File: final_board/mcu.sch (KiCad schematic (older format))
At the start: 9 parts, among them U402 MCP2551-I/SN, U403 LPC11C14

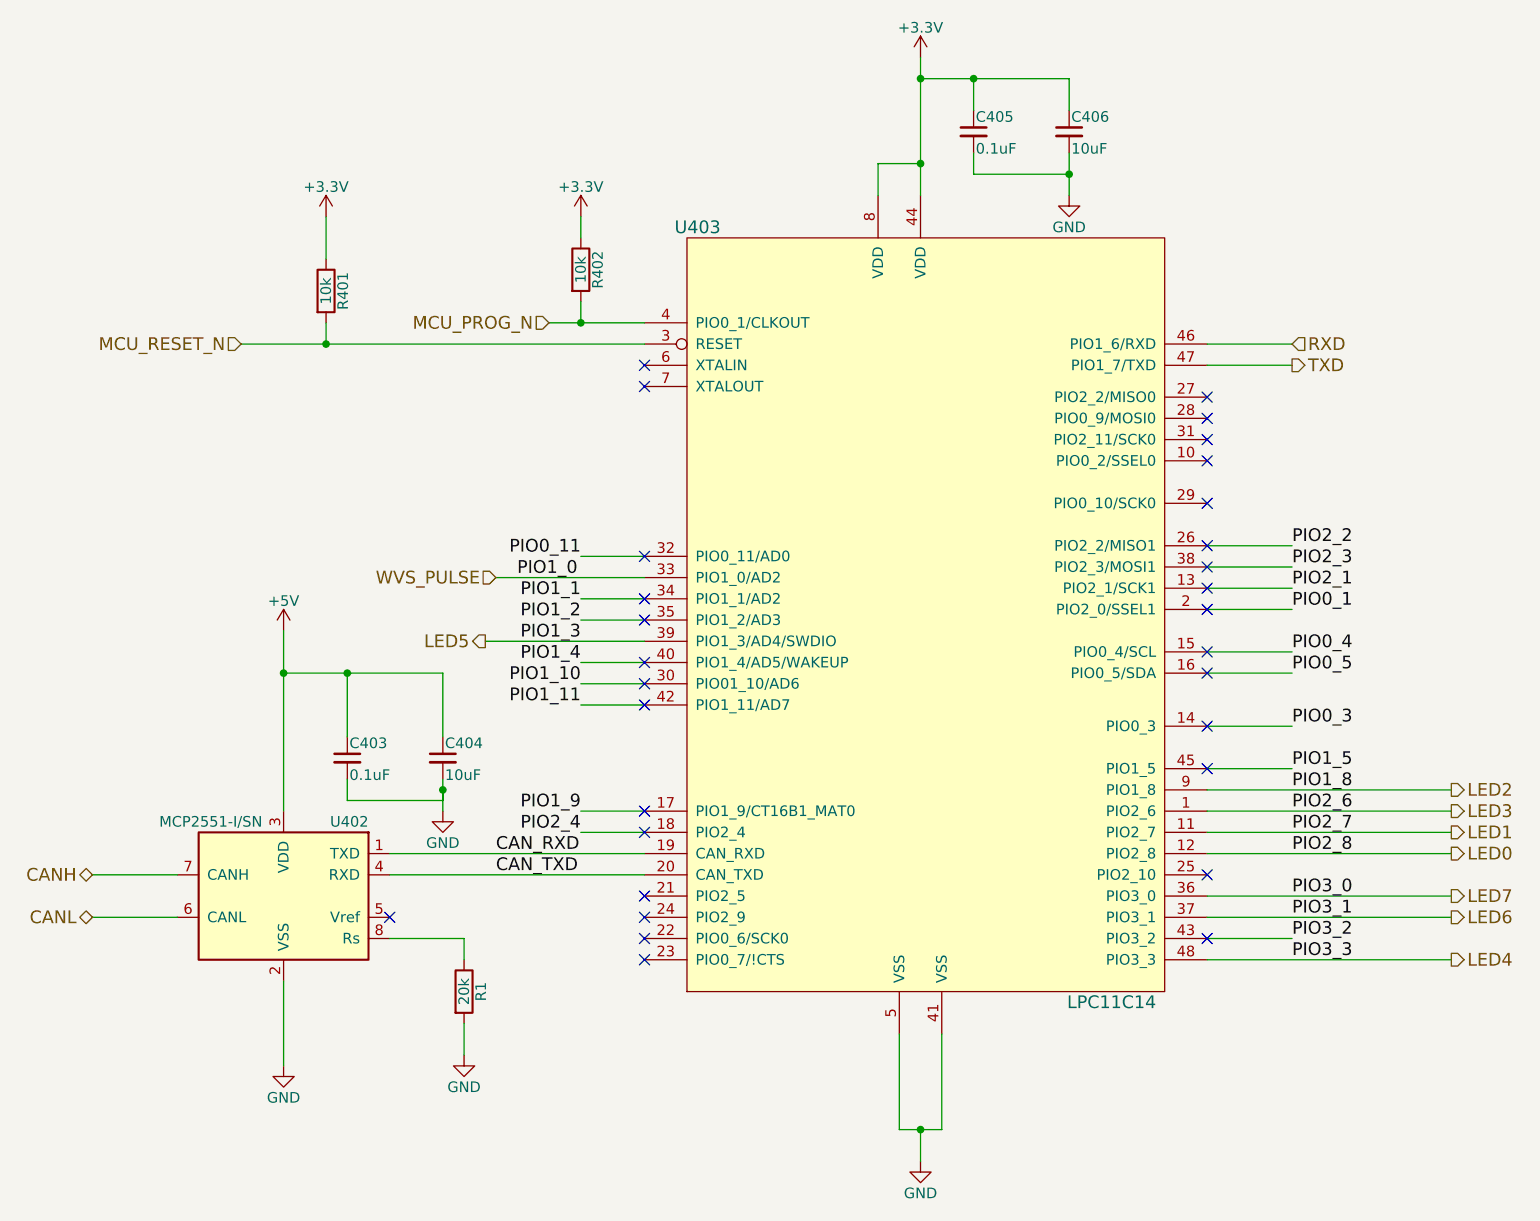
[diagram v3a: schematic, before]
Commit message: Updated PCB by replacing old parts, fixing voltage regulator, adding test points, and general improvements
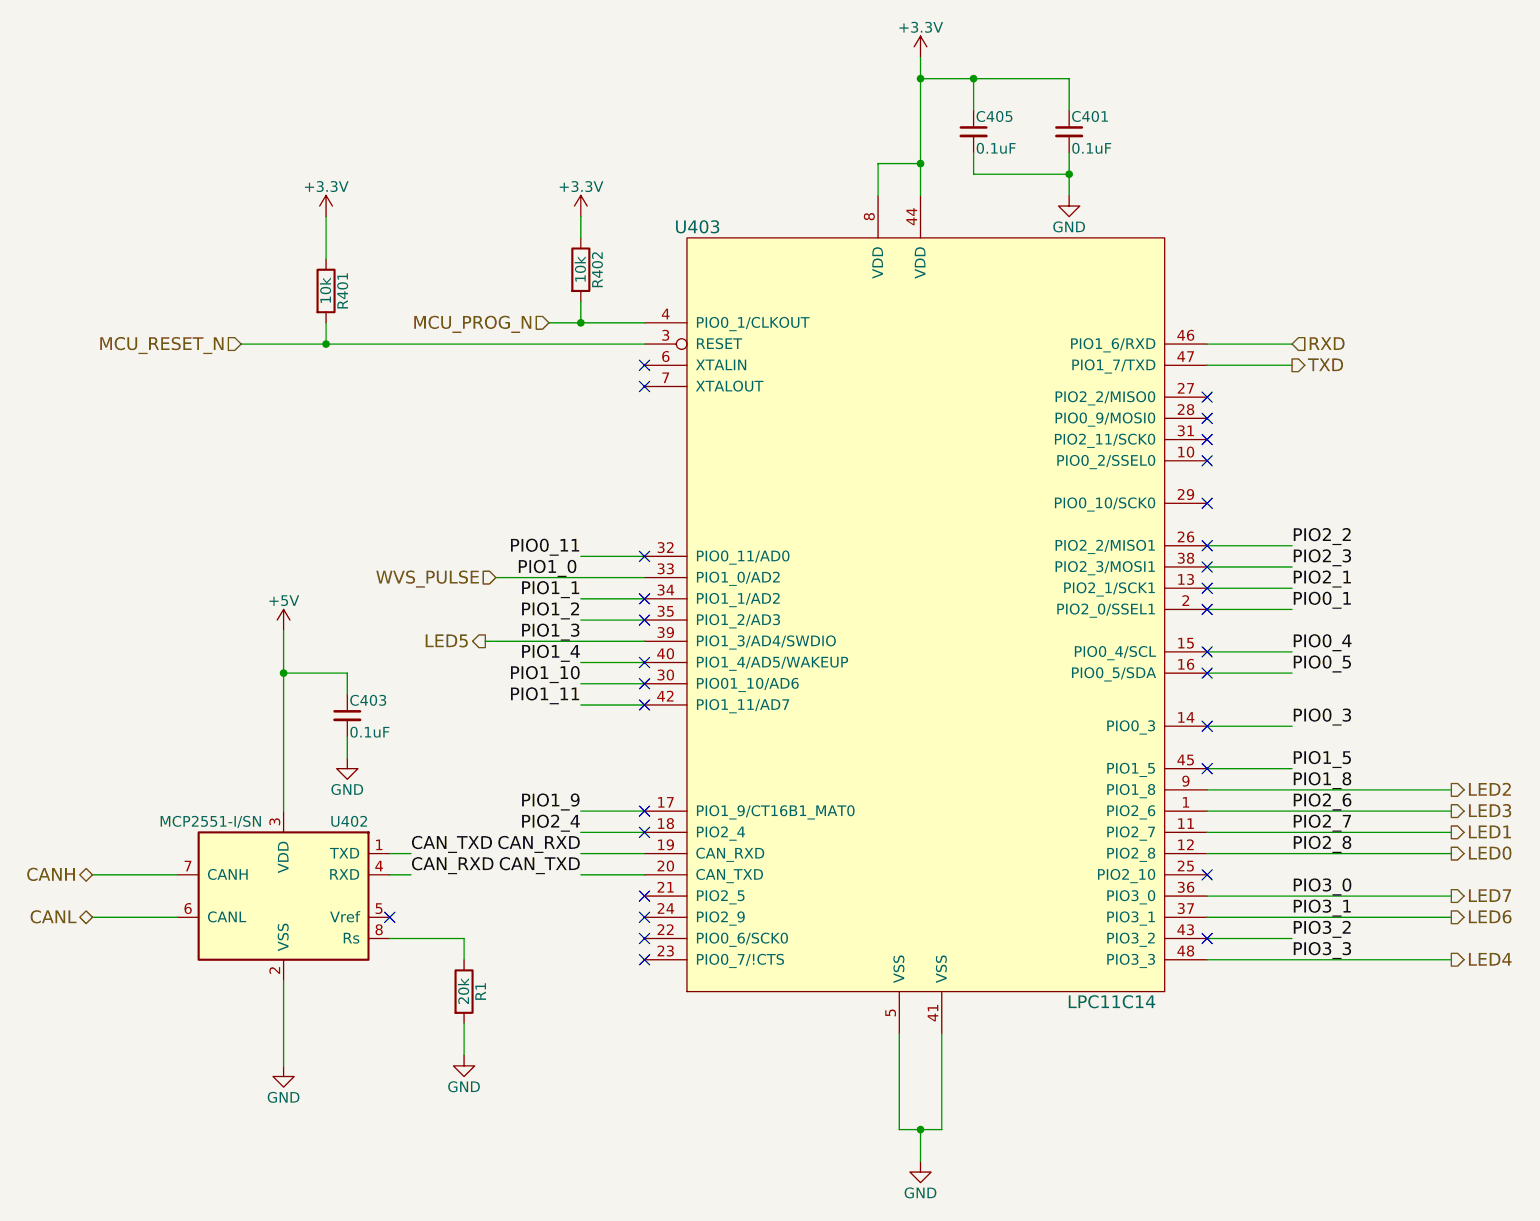
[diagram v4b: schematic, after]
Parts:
- removed C404, C406: 10uF, Capacitors_SMD:C_0805_HandSoldering, symbol C_Small
- added C401: 0.1uF, Capacitors_SMD:C_0603_HandSoldering, symbol C_Small
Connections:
- net +3V3: now also C401.1
- net CAN_RXD: now also U402.4 (RXD); no longer U402.1 (TXD)
- net CAN_TXD: now also U402.1 (TXD); no longer U402.4 (RXD)
- net GND: now also C401.2
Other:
- moved on the sheet: C403
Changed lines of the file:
@@
 CANH
 $Comp
-L GND #PWR09
+L GND #PWR017
 U 1 1 563E2693
 P 4100 5700
-F 0 "#PWR09" H 4100 5450 50  0001 C CNN
+F 0 "#PWR017" H 4100 5450 50  0001 C CNN
 F 1 "GND" H 4100 5550 50  0000 C CNN
 F 2 "" H 4100 5700 60  0000 C CNN
@@
 $EndComp
 $Comp
-L GND #PWR010
+L GND #PWR018
 U 1 1 563E26E3
 P 3250 5750
-F 0 "#PWR010" H 3250 5500 50  0001 C CNN
+F 0 "#PWR018" H 3250 5500 50  0001 C CNN
 F 1 "GND" H 3250 5600 50  0000 C CNN
 F 2 "" H 3250 5750 60  0000 C CNN
@@
 L C_Small C403
 U 1 1 563E286E
+P 3550 4100
+F 0 "C403" H 3560 4170 50  0000 L CNN
+F 1 "0.1uF" H 3560 4020 50  0000 L CNN
+F 2 "Capacitors_SMD:C_0603_HandSoldering" H 3550 4100 60  0001 C CNN
+F 3 "" H 3550 4100 60  0000 C CNN
+	1    3550 4100
+	1    0    0    -1
+$EndComp
+$Comp
+L GND #PWR019
+U 1 1 563E2AAC
 P 3550 4300
-F 0 "C403" H 3560 4370 50  0000 L CNN
-F 1 "0.1uF" H 3560 4220 50  0000 L CNN
-F 2 "Capacitors_SMD:C_0603_HandSoldering" H 3550 4300 60  0001 C CNN
+F 0 "#PWR019" H 3550 4050 50  0001 C CNN
+F 1 "GND" H 3550 4150 50  0000 C CNN
+F 2 "" H 3550 4300 60  0000 C CNN
 F 3 "" H 3550 4300 60  0000 C CNN
 	1    3550 4300
-	1    0    0    -1
-$EndComp
-$Comp
-L C_Small C404
-U 1 1 563E28A1
-P 4000 4300
-F 0 "C404" H 4010 4370 50  0000 L CNN
-F 1 "10uF" H 4010 4220 50  0000 L CNN
-F 2 "Capacitors_SMD:C_0805_HandSoldering" H 4000 4300 60  0001 C CNN
-F 3 "" H 4000 4300 60  0000 C CNN
-	1    4000 4300
-	1    0    0    -1
-$EndComp
-$Comp
-L GND #PWR011
-U 1 1 563E2AAC
-P 4000 4550
-F 0 "#PWR011" H 4000 4300 50  0001 C CNN
-F 1 "GND" H 4000 4400 50  0000 C CNN
-F 2 "" H 4000 4550 60  0000 C CNN
-F 3 "" H 4000 4550 60  0000 C CNN
-	1    4000 4550
 	1    0    0    -1
 $EndComp
@@
 PIO2_4
 $Comp
-L GND #PWR012
+L GND #PWR020
 U 1 1 563E497F
 P 6250 6200
-F 0 "#PWR012" H 6250 5950 50  0001 C CNN
+F 0 "#PWR020" H 6250 5950 50  0001 C CNN
 F 1 "GND" H 6250 6050 50  0000 C CNN
 F 2 "" H 6250 6200 60  0000 C CNN
@@
 $EndComp
 $Comp
-L C_Small C406
-U 1 1 563E4C7A
-P 6950 1350
-F 0 "C406" H 6960 1420 50  0000 L CNN
-F 1 "10uF" H 6960 1270 50  0000 L CNN
-F 2 "Capacitors_SMD:C_0805_HandSoldering" H 6950 1350 60  0001 C CNN
-F 3 "" H 6950 1350 60  0000 C CNN
-	1    6950 1350
-	1    0    0    -1
-$EndComp
-$Comp
-L GND #PWR013
+L GND #PWR021
 U 1 1 563E4F46
 P 6950 1650
-F 0 "#PWR013" H 6950 1400 50  0001 C CNN
+F 0 "#PWR021" H 6950 1400 50  0001 C CNN
 F 1 "GND" H 6950 1500 50  0000 C CNN
 F 2 "" H 6950 1650 60  0000 C CNN
@@
 LED0
 $Comp
-L +3.3V #PWR014
+L +3.3V #PWR022
 U 1 1 5647852E
 P 3450 1750
-F 0 "#PWR014" H 3450 1600 50  0001 C CNN
+F 0 "#PWR022" H 3450 1600 50  0001 C CNN
 F 1 "+3.3V" H 3450 1890 50  0000 C CNN
 F 2 "" H 3450 1750 60  0000 C CNN
@@
 $EndComp
 $Comp
-L +3.3V #PWR015
+L +3.3V #PWR023
 U 1 1 56478628
 P 4650 1750
-F 0 "#PWR015" H 4650 1600 50  0001 C CNN
+F 0 "#PWR023" H 4650 1600 50  0001 C CNN
 F 1 "+3.3V" H 4650 1890 50  0000 C CNN
 F 2 "" H 4650 1750 60  0000 C CNN
@@
 $EndComp
 $Comp
-L +3.3V #PWR016
+L +3.3V #PWR024
 U 1 1 56478697
 P 6250 1000
-F 0 "#PWR016" H 6250 850 50  0001 C CNN
+F 0 "#PWR024" H 6250 850 50  0001 C CNN
 F 1 "+3.3V" H 6250 1140 50  0000 C CNN
 F 2 "" H 6250 1000 60  0000 C CNN
@@
 	1    0    0    -1
 $EndComp
-Text Label 4250 4750 0    60   ~ 0
+Text Label 4650 4750 2    60   ~ 0
 CAN_RXD
-Text Label 4250 4850 0    60   ~ 0
+Text Label 4650 4850 2    60   ~ 0
 CAN_TXD
 Text Label 4650 3750 2    60   ~ 0
 PIO1_3
-Wire Wire Line
-	3750 4750 4950 4750
-Wire Wire Line
-	3750 4850 4950 4850
-Wire Wire Line
-	2350 4850 2750 4850
-Wire Wire Line
-	2350 5050 2750 5050
-Wire Wire Line
-	3250 3700 3250 4550
-Wire Wire Line
-	3550 3900 3550 4200
-Wire Wire Line
-	4000 3900 4000 4200
-Connection ~ 3550 3900
-Wire Wire Line
-	3550 4400 3550 4500
-Wire Wire Line
-	3550 4500 4000 4500
-Wire Wire Line
-	4000 4500 4000 4400
-Wire Wire Line
-	4000 4450 4000 4550
-Connection ~ 4000 4450
-Connection ~ 3250 3900
-Wire Wire Line
-	4950 4050 4650 4050
-Wire Wire Line
-	4650 3950 4950 3950
-Wire Wire Line
-	4650 3350 4950 3350
-Wire Wire Line
-	4250 3450 4950 3450
-Wire Wire Line
-	4650 3550 4950 3550
-Wire Wire Line
-	4650 3650 4950 3650
-Wire Wire Line
-	4200 3750 4950 3750
-Wire Wire Line
-	4650 3850 4950 3850
-Wire Wire Line
-	4500 2250 4950 2250
-Wire Wire Line
-	4650 2150 4650 2250
-Connection ~ 4650 2250
-Wire Wire Line
-	4650 1850 4650 1750
-Wire Wire Line
-	3050 2350 4950 2350
-Wire Wire Line
-	3450 2250 3450 2350
-Connection ~ 3450 2350
-Wire Wire Line
-	3450 1750 3450 1950
-Wire Wire Line
-	4650 4550 4950 4550
-Wire Wire Line
-	4650 4650 4950 4650
-Wire Wire Line
-	6150 5600 6150 6050
-Wire Wire Line
-	6150 6050 6350 6050
-Wire Wire Line
-	6350 6050 6350 5600
-Wire Wire Line
-	6250 6050 6250 6200
-Connection ~ 6250 6050
-Wire Wire Line
-	6250 1000 6250 1650
-Wire Wire Line
-	6050 1650 6050 1500
-Wire Wire Line
-	6050 1500 6250 1500
-Connection ~ 6250 1500
-Wire Wire Line
-	6250 1100 6950 1100
-Wire Wire Line
-	6950 1100 6950 1250
-Connection ~ 6250 1100
-Wire Wire Line
-	6500 1250 6500 1100
-Connection ~ 6500 1100
-Wire Wire Line
-	6950 1450 6950 1650
-Wire Wire Line
-	6950 1550 6500 1550
-Wire Wire Line
-	6500 1550 6500 1450
-Connection ~ 6950 1550
-Wire Wire Line
-	8000 2350 7600 2350
-Wire Wire Line
-	8000 2450 7600 2450
-Wire Wire Line
-	8000 3300 7600 3300
-Wire Wire Line
-	7600 3400 8000 3400
-Wire Wire Line
-	7600 3500 8000 3500
-Wire Wire Line
-	7600 3600 8000 3600
-Wire Wire Line
-	8000 3800 7600 3800
-Wire Wire Line
-	8000 3900 7600 3900
-Wire Wire Line
-	8000 4150 7600 4150
-Wire Wire Line
-	8000 4350 7600 4350
-Wire Wire Line
-	7600 4450 8750 4450
-Wire Wire Line
-	7600 4550 8750 4550
-Wire Wire Line
-	7600 4650 8750 4650
-Wire Wire Line
-	7600 4750 8750 4750
-Wire Wire Line
-	7600 4950 8750 4950
-Wire Wire Line
-	7600 5050 8750 5050
-Wire Wire Line
-	7600 5150 8000 5150
-Wire Wire Line
-	7600 5250 8750 5250
 Text HLabel 4250 3450 0    60   Input ~ 0
 WVS_PULSE
@@
 	-1   0    0    -1
 $EndComp
-Wire Wire Line
-	3250 5350 3250 5750
-Wire Wire Line
-	3250 3900 4000 3900
 $Comp
 L R R1
@@
 	1    0    0    -1
 $EndComp
-Wire Wire Line
-	4100 5550 4100 5700
 NoConn ~ 3750 5050
-Wire Wire Line
-	3750 5150 4100 5150
-Wire Wire Line
-	4100 5150 4100 5250
-$Comp
-L +5V #PWR017
+$Comp
+L +5V #PWR025
 U 1 1 56917D77
 P 3250 3700
-F 0 "#PWR017" H 3250 3550 50  0001 C CNN
+F 0 "#PWR025" H 3250 3550 50  0001 C CNN
 F 1 "+5V" H 3250 3840 50  0000 C CNN
 F 2 "" H 3250 3700 50  0000 C CNN
@@
 NoConn ~ 4950 3550
 NoConn ~ 4950 3350
+$Comp
+L C_Small C401
+U 1 1 5825915E
+P 6950 1350
+F 0 "C401" H 6960 1420 50  0000 L CNN
+F 1 "0.1uF" H 6960 1270 50  0000 L CNN
+F 2 "Capacitors_SMD:C_0603_HandSoldering" H 6950 1350 50  0001 C CNN
+F 3 "" H 6950 1350 50  0000 C CNN
+	1    6950 1350
+	1    0    0    -1
+$EndComp
+Wire Wire Line
+	2350 4850 2750 4850
+Wire Wire Line
+	2350 5050 2750 5050
+Wire Wire Line
+	3250 3700 3250 4550
+Connection ~ 3250 3900
+Wire Wire Line
+	4950 4050 4650 4050
+Wire Wire Line
+	4650 3950 4950 3950
+Wire Wire Line
+	4650 3350 4950 3350
+Wire Wire Line
+	4250 3450 4950 3450
+Wire Wire Line
+	4650 3550 4950 3550
+Wire Wire Line
+	4650 3650 4950 3650
+Wire Wire Line
+	4200 3750 4950 3750
+Wire Wire Line
+	4650 3850 4950 3850
+Wire Wire Line
+	4500 2250 4950 2250
+Wire Wire Line
+	4650 2150 4650 2250
+Connection ~ 4650 2250
+Wire Wire Line
+	4650 1850 4650 1750
+Wire Wire Line
+	3050 2350 4950 2350
+Wire Wire Line
+	3450 2250 3450 2350
+Connection ~ 3450 2350
+Wire Wire Line
+	3450 1750 3450 1950
+Wire Wire Line
+	4650 4550 4950 4550
+Wire Wire Line
+	4650 4650 4950 4650
+Wire Wire Line
+	6150 5600 6150 6050
+Wire Wire Line
+	6150 6050 6350 6050
+Wire Wire Line
+	6350 6050 6350 5600
+Wire Wire Line
+	6250 6050 6250 6200
+Connection ~ 6250 6050
+Wire Wire Line
+	6250 1000 6250 1650
+Wire Wire Line
+	6050 1650 6050 1500
+Connection ~ 6250 1500
+Connection ~ 6250 1100
+Wire Wire Line
+	6500 1250 6500 1100
+Wire Wire Line
+	6500 1550 6500 1450
+Connection ~ 6950 1550
+Wire Wire Line
+	8000 2350 7600 2350
+Wire Wire Line
+	8000 2450 7600 2450
+Wire Wire Line
+	8000 3300 7600 3300
+Wire Wire Line
+	7600 3400 8000 3400
+Wire Wire Line
+	7600 3500 8000 3500
+Wire Wire Line
+	7600 3600 8000 3600
+Wire Wire Line
+	8000 3800 7600 3800
+Wire Wire Line
+	8000 3900 7600 3900
+Wire Wire Line
+	8000 4150 7600 4150
+Wire Wire Line
+	8000 4350 7600 4350
+Wire Wire Line
+	7600 4450 8750 4450
+Wire Wire Line
+	7600 4550 8750 4550
+Wire Wire Line
+	7600 4650 8750 4650
+Wire Wire Line
+	7600 4750 8750 4750
+Wire Wire Line
+	7600 4950 8750 4950
+Wire Wire Line
+	7600 5050 8750 5050
+Wire Wire Line
+	7600 5150 8000 5150
+Wire Wire Line
+	7600 5250 8750 5250
+Wire Wire Line
+	3250 5350 3250 5750
+Wire Wire Line
+	4100 5550 4100 5700
+Wire Wire Line
+	3750 5150 4100 5150
+Wire Wire Line
+	4100 5150 4100 5250
+Wire Wire Line
+	6950 1100 6950 1250
+Wire Wire Line
+	6950 1450 6950 1650
+Wire Wire Line
+	6500 1550 6950 1550
+Wire Wire Line
+	6250 1100 6950 1100
+Connection ~ 6500 1100
+Wire Wire Line
+	3550 3900 3250 3900
+Wire Wire Line
+	3550 4300 3550 4200
+Wire Wire Line
+	3550 4000 3550 3900
+Wire Wire Line
+	6050 1500 6250 1500
+Wire Wire Line
+	4950 4850 4650 4850
+Wire Wire Line
+	4950 4750 4650 4750
+Text Label 3850 4750 0    60   ~ 0
+CAN_TXD
+Text Label 3850 4850 0    60   ~ 0
+CAN_RXD
+Wire Wire Line
+	3850 4750 3750 4750
+Wire Wire Line
+	3750 4850 3850 4850
 $EndSCHEMATC
